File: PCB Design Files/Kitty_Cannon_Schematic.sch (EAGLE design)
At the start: 11 parts, among them J1 DCJ200-10-A-XX-X_REVA, J2 RASPBERRYPI-40-PIN-GPIO_PTH, J3 DCJ200-10-A-XX-X_REVA, J4 DCJ200-10-A-XX-X_REVA, J5 USB1040-XX-X-X_REVC, U1 LD1085V50

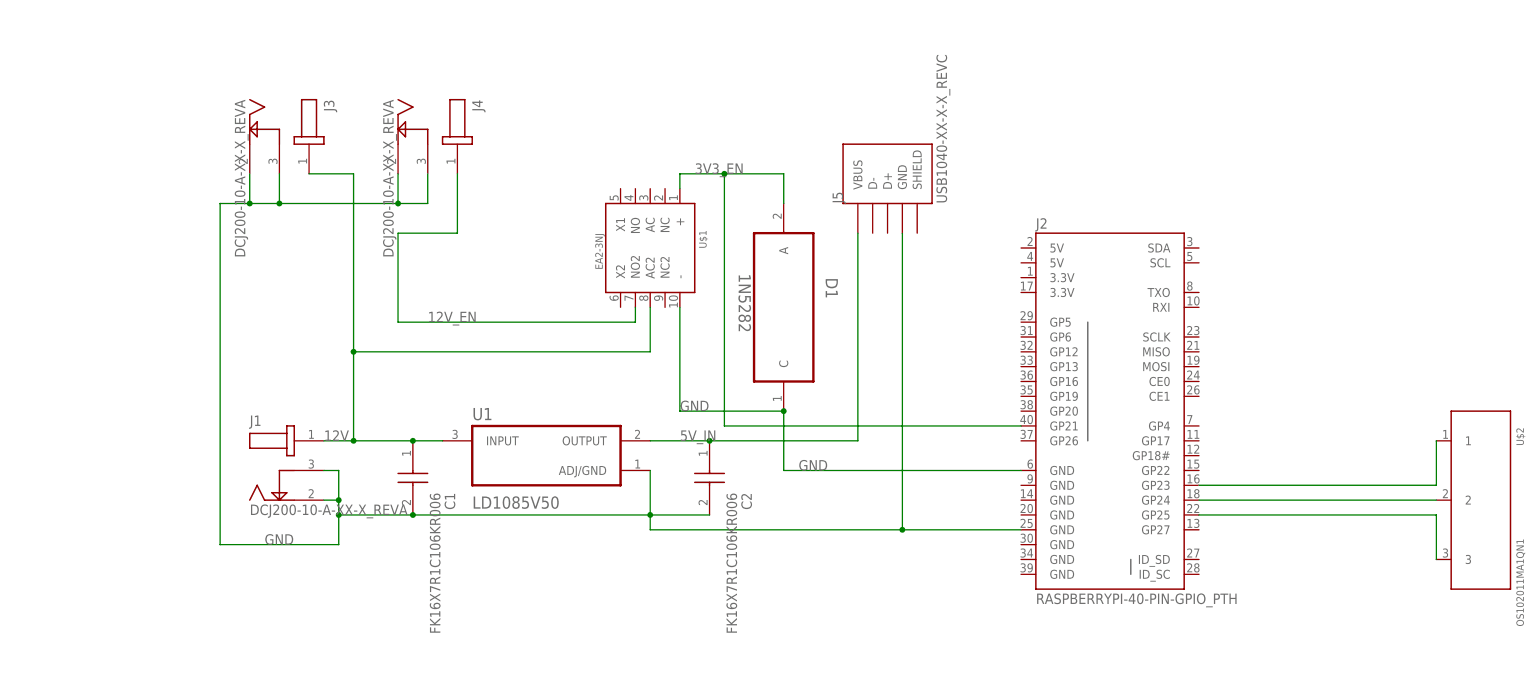
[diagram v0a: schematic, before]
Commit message: Kitty Cannon - update structure
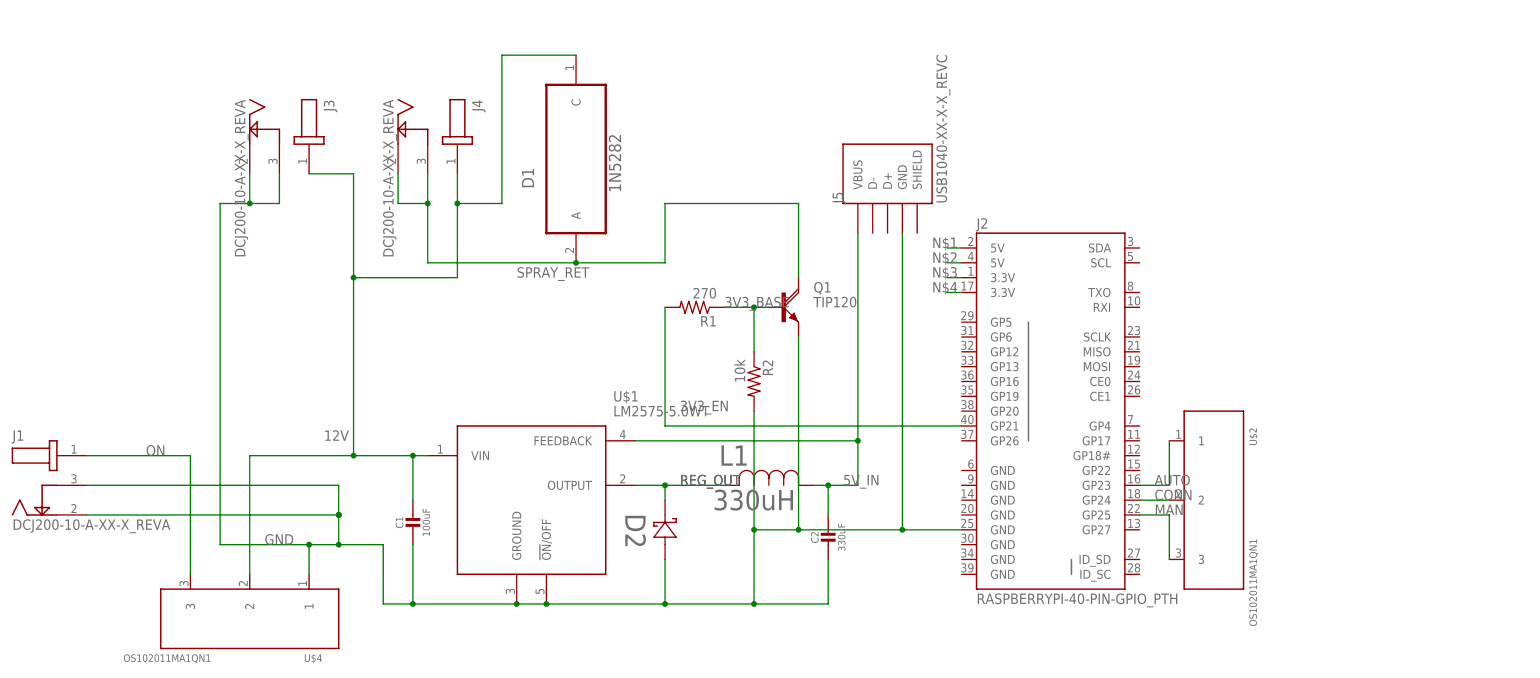
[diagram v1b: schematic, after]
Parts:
- removed U1: LD1085V50, LD1085V50:LD1085V50
- added D2: SB3100E-G, SB3100E-G_Schottky:SB3100E-G
- added L1: 330uH, 1433428C_330uH:1433428C
- added Q1: TIP120, transistor-power:TIP120
- added R1: 270, rcl:R-US_0204/5
- added R2: 10k, rcl:R-US_0204/5
- added U$4: OS102011MA1QN1, C&K:OS102011MA1QN1
- C1: value FK16X7R1C106KR006 -> 100uF; device FK16X7R1C106KR006:FK16X7R1C106KR006 -> 860010372006_100uF:860010372006_100UF
- C2: value FK16X7R1C106KR006 -> 330uF; device FK16X7R1C106KR006:FK16X7R1C106KR006 -> 860010372006_100uF:860010372006_100UF
- U$1: value EA2-3NJ -> LM2575-5.0WT; device Kemet:EA2-3NJ -> LM2575-5.0WT:LM2575-5.0WT
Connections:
- net N$1 renamed MAN
- net N$2 renamed AUTO
- net N$7 renamed CONN
- removed net 12V_EN: J4.1, U$1.NO2
- new net 3V3_BASE: Q1.B, R1.1, R2.1
- new net N$1: J2.5V@2
- new net N$2: J2.5V@4
- new net N$3: J2.3.3V@1
- new net N$4: J2.3.3V@17
- new net ON: J1.1, U$4.3
- new net REG_OUT: D2.1, L1.2, U$1.OUTPUT
- new net SPRAY_RET: D1.A, J4.2, J4.3, Q1.C
- net 12V: now also D1.C, J4.1, U$1.VIN, U$4.2; no longer J1.1, U$1.AC2, U1.INPUT
- net 3V3_EN: now also R1.2; no longer D1.A, U$1.+
- net 5V_IN: now also L1.1, U$1.FEEDBACK; no longer U1.OUTPUT
- net GND: now also D2.2, Q1.E, R2.2, U$1.!ON!/OFF, U$1.GROUND, U$4.1; no longer D1.C, J2.GND@6, J4.2, J4.3, U$1.-, U1.ADJ/GND
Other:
- moved on the sheet: D1, J1, J2, U$2
